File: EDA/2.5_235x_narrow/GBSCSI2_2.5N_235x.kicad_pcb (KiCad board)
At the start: 4 copper layers, 69.5 x 93.5 mm, 145 parts, among them J1 SCSI_50-2P_2mm, J1.1 SCSI_50P_2.54mm, J2 TF003, J3 GCT-4105, J4 SM03B-SRSS-TB, J4.1 Conn_01x04, J5 Conn_01x04, J6 Conn_01x02, Q1 AO3401A, Q10 AO3401A, Q11 AO3401A, Q12 AO3401A, Q13 AO3401A, Q14 AO3401A, Q15 AO3401A, Q16 AO3401A, Q17 AO3401A, Q18 AO3401A, Q2 AO3401A, Q3 AO3401A, Q4 AO3401A, Q5 AO3401A, Q6 AO3401A, Q7 AO3401A, Q8 AO3401A, Q9 AO3401A, SW1 SW_DIP_x04, U1 RP2350_60QFN, U10 AZ1117-2.85, U2 W25Q128JVS, U3 USB TVS, U4 74LVTH245, U5 74LVTH245, U6 74LVTH125, U7 74LVTH125, U8 SN74AHC1G125DBVR, U9 TLV62569DBV, Y1 12MHz

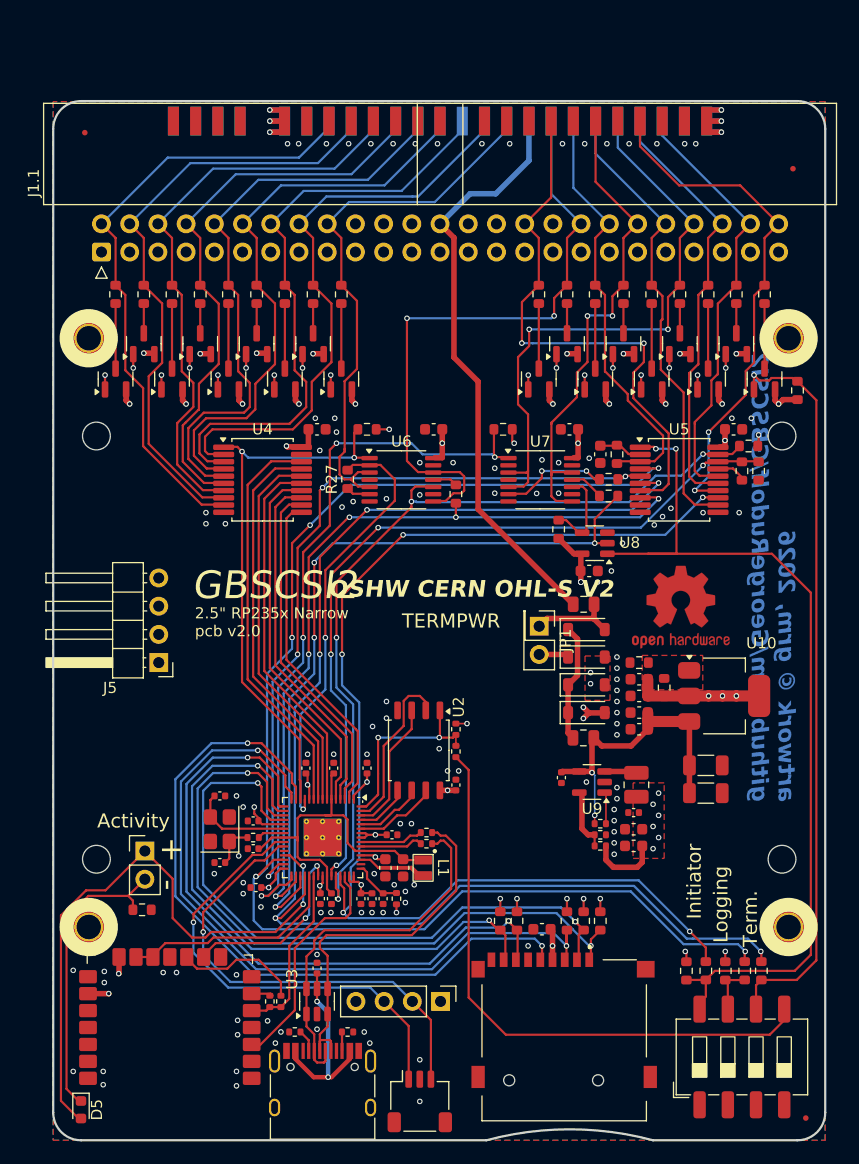
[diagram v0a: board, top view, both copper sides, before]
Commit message: Tidying up PCB footprint slightly, more work needed, ERC passes on narrow variants
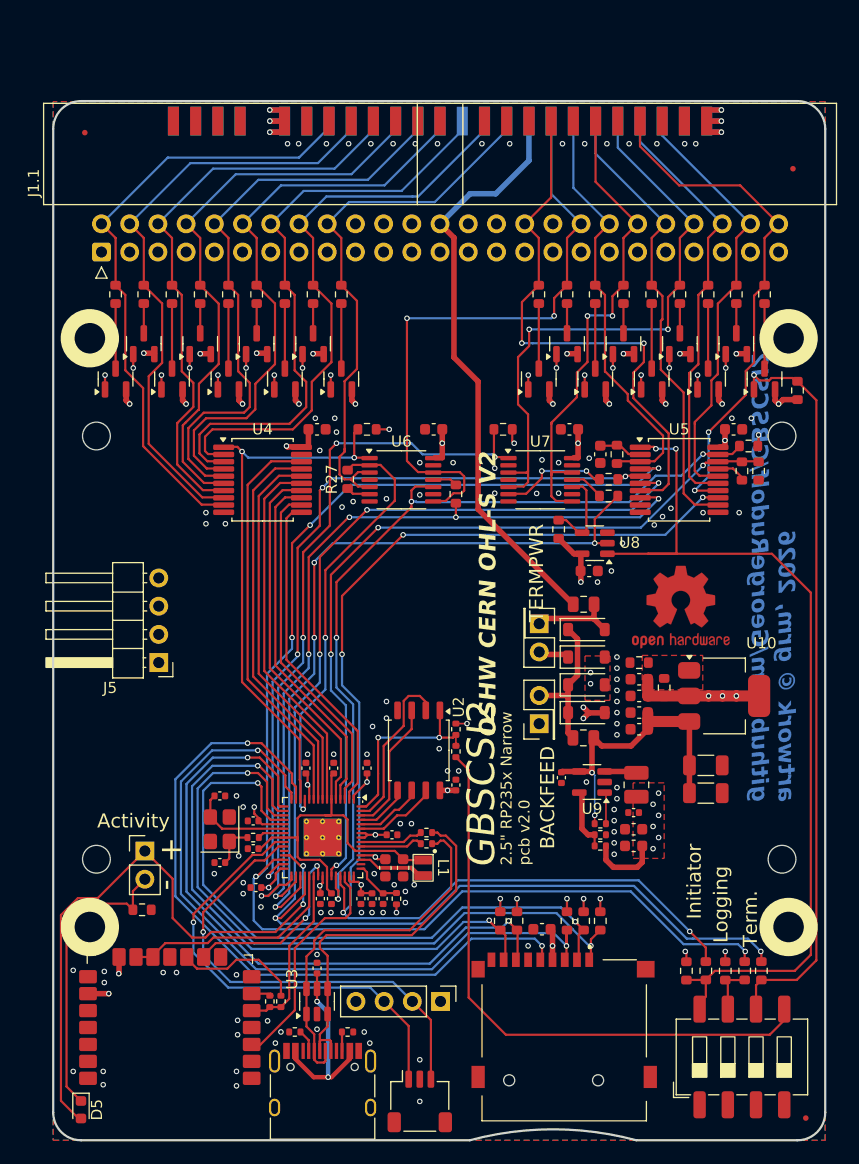
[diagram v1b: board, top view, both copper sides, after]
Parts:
- added JP2: Jumper_2_Open, Connector_PinHeader_2.54mm:PinHeader_2x01_P2.54mm_Vertical, F.Cu at (79.2, 105.0)
- C10: value 4.7uF -> 4.7μF
- C20, C35: value 47uF -> 47μF
- moved JP1 0.22 mm to (79.2, 96.0)
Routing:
- net +5VIN: track 200.9 -> 208.5 mm
- net /Power/5V_TIE: track 10.6 -> 13.3 mm
- net +3.3V: vias 36 -> 35
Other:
- outline, holes or cut-outs redrawn
- board text added: "BACKFEED"

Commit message: Prettifying models
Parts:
- U1: footprint Package_DFN_QFN:QFN-60-1EP_7x7mm_P0.4mm_EP3.4x3.4mm_ThermalVias -> GBSCSI:RP2350-QFN-60-1EP_7x7_P0.4mm_EP3.4x3.4mm_ThermalVias
- moved C1 7.00 mm to (65.4, 111.0)
- moved C10 7.00 mm to (60.5, 113.8)
- moved C11 7.00 mm to (53.5, 109.2)
- moved C12 7.00 mm to (64.2, 113.8)
- moved C13 7.00 mm to (63.8, 102.0)
- moved C14 7.00 mm to (58.2, 102.0)
- moved C15 7.00 mm to (53.5, 106.8)
- moved C16 7.00 mm to (53.8, 112.8)
- moved C17 7.00 mm to (59.5, 113.8)
- moved C18 7.00 mm to (63.2, 113.8)
- moved C19 7.00 mm to (66.0, 108.0)
- moved C2 7.00 mm to (50.5, 104.5)
- moved C20 7.00 mm to (94.2, 104.2)
- moved C21 7.00 mm to (84.8, 73.8)
- moved C22 7.00 mm to (59.2, 71.5)
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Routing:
- net VBUS: track 111.8 -> 66.4 mm, vias 4 -> 5
- net +5VIN: track 208.5 -> 189.7 mm
- net +2.8V: track 192.4 -> 181.4 mm
- net GND: track 0.00 -> 7.85 mm
- added copper zone on B.Cu, net +3.3V
- added copper zone on In2.Cu, net GND
- removed copper zone on In2.Cu, net +3.3V
- removed copper zone on B.Cu, net GND
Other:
- board text added: "USB Boot"

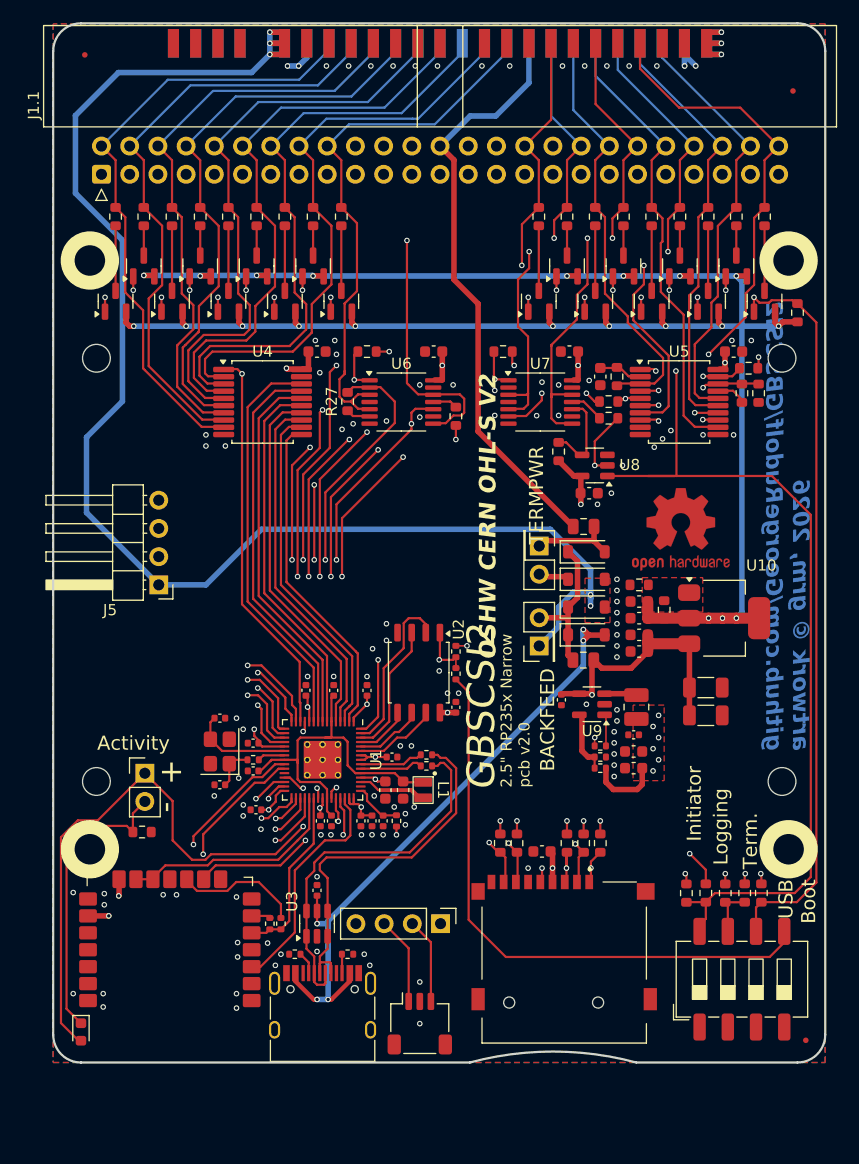
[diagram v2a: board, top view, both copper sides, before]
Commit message: Fixing PCB footprint
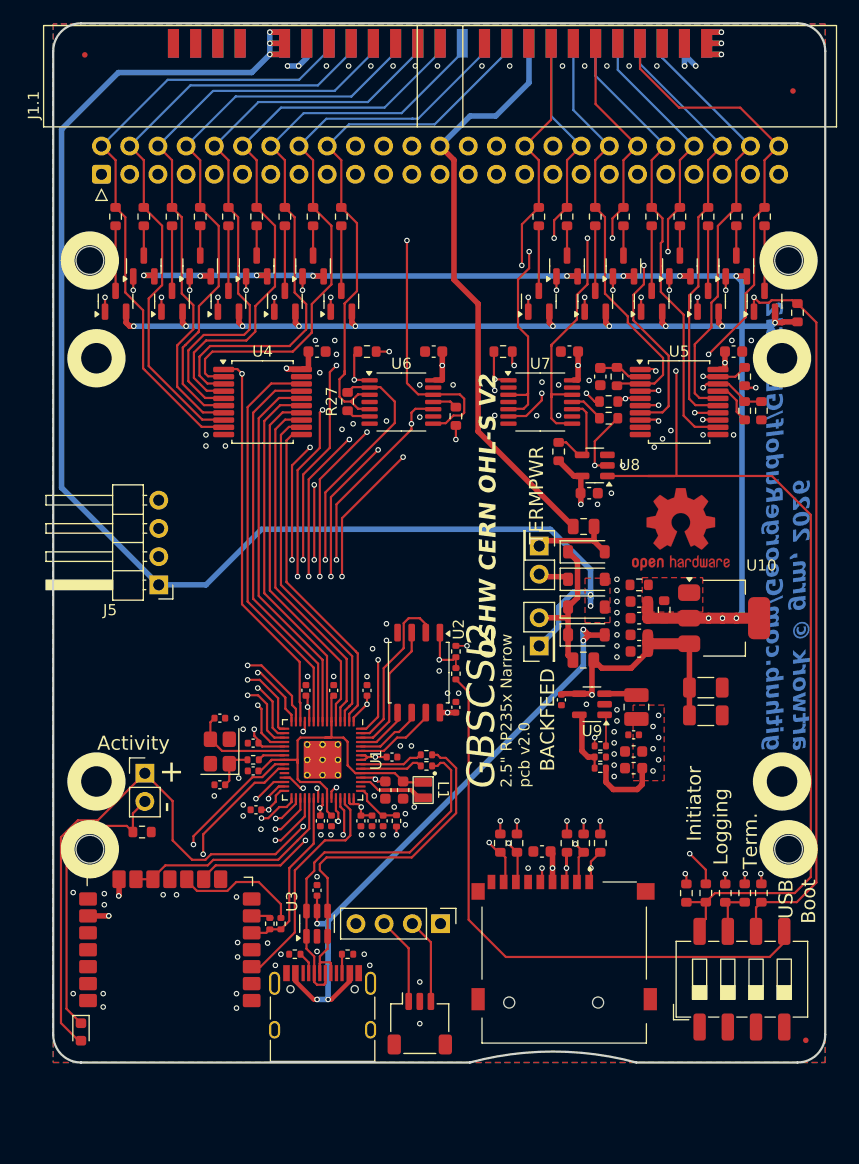
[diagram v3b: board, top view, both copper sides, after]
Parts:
- moved R17 1.59 mm to (99.2, 76.8)
- moved R26 1.59 mm to (97.8, 76.8)
- moved R6 0.83 mm to (97.8, 73.8), turned to 90 degrees
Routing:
- net Net-(U5-B1): track 2.33 -> 4.07 mm
- net +5VIN: track 189.7 -> 188.1 mm
- net /Core Logic, Basic Controls/~{MCU_ACK}: track 71.1 -> 72.1 mm

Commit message: Resuming work
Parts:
- C2, C3: value 22pF -> 15pF
- U1: value RP2350_60QFN -> RP235x_60QFN
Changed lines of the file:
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@@
 			)
 		)
-		(property "LCSC" "N/A"
-			(at 66.24 -72.2 0)
-			(unlocked yes)
-			(layer "F.Fab")
-			(hide yes)
-			(effects
-				(font
-					(size 1 1)
-					(thickness 0.15)
-				)
-			)
-		)
-		(property "LCSC Part #" "N/A"
-			(at 66.24 -72.2 0)
-			(layer "F.Fab")
-			(hide yes)
-			(effects
-				(font
-					(size 1 1)
-					(thickness 0.15)
-				)
-			)
-		)
 		(sheetname "/")
 		(sheetfile "GBSCSI2_2.5N_235x.kicad_sch")
@@
 		(model "${KIPRJMOD}/../../EDA/Libraries/3D_models/sm03b-srss-tb_connector.step"
 			(offset
-				(xyz 0 1.5 0)
+				(xyz 0 1.5 -0.5)
 			)
 			(scale
@@
 		(sheetname "/Core Logic, Basic Controls/")
 		(sheetfile "../Common Sheets/core_235xA_narrow.kicad_sch")
-		(attr smd)
+		(attr smd dnp)
 		(fp_line
 			(start -2.725 2.725)
@@
 			)
 		)
-		(property "LCSC" "C133334"
+		(property "LCSC" "C20625731"
 			(at 0 0 90)
 			(unlocked yes)
@@
 			)
 		)
-		(property "Preferred MPN" "TAXM12M4RLBDDT2T"
+		(property "Preferred MPN" "ABM8-272-T3 "
 			(at 0 0 90)
 			(unlocked yes)
@@
 			)
 		)
-		(property "Alternate Part Number" "TX322512M4LBCE2T"
+		(property "Alternate Part Number" "TAXM12M4RLBDDT2T"
 			(at 0 0 90)
 			(unlocked yes)
@@
 			)
 		)
-		(property "Nominal Preferred Characteristics" "Cl=20pF - adjustments change C2/C3, ESR=50Ω"
+		(property "Nominal Preferred Characteristics" "Cl=10pF - adjustments change C2/C3, ESR=50Ω"
 			(at 0 0 90)
 			(unlocked yes)
@@
 			)
 		)
-		(property "Value" "RP2350_60QFN"
+		(property "Value" "RP235x_60QFN"
 			(at 0 4.82 270)
 			(layer "F.Fab")
@@
 			)
 		)
-		(property "LCSC" "C42411118"
+		(property "LCSC" "C41378174"
 			(at 0 0 270)
 			(unlocked yes)
@@
 			)
 		)
-		(property "Value" "22pF"
+		(property "Value" "15pF"
 			(at 0 1.16 0)
 			(layer "F.Fab")
@@
 			)
 		)
-		(property "LCSC" "C1555"
+		(property "LCSC" "C1548"
 			(at 0 0 180)
 			(unlocked yes)
@@
 			)
 		)
-		(property "Preferred MPN" "0402CG220J500NT"
+		(property "Preferred MPN" "0402CG150J500NT"
 			(at 0 0 180)
 			(unlocked yes)
@@
 			)
 		)
-		(property "Value" "22pF"
+		(property "Value" "15pF"
 			(at 0 1.16 0)
 			(layer "F.Fab")
@@
 			)
 		)
-		(property "LCSC" "C1555"
+		(property "LCSC" "C1548"
 			(at 0 0 0)
 			(unlocked yes)
@@
 			)
 		)
-		(property "Preferred MPN" "0402CG220J500NT"
+		(property "Preferred MPN" "0402CG150J500NT"
 			(at 0 0 0)
 			(unlocked yes)
